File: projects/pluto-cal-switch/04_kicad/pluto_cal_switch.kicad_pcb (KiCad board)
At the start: 4 copper layers, 112 x 60 mm, 77 parts, among them Y1 C20625731

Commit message: the 50 ohm width was one method run twice, and the term that decides it is the solder mask nobody counted
RE-DERIVED INDEPENDENTLY BEFORE AUTHORING, because both existing
derivations were Hammerstad-Jensen closed form — one method twice, which
is the shared-method trap canon M1 names, not two agreeing sources.

METHOD: 2D finite-difference electrostatic field solve on the actual
cross-section. Box-integration discretisation of div(eps grad V)=0 on a
graded half-domain with a Neumann symmetry plane; charge by DISCRETE
GAUSS (Q = -eps0 * (A@V) over the conductor nodes), cross-checked against
the field-energy integral (agree to 1e-3). VALIDATED at t=0 against
Hammerstad-Jensen — where the closed form is uncontroversial — to
-0.29..-0.56 % over w/h 0.5..4.0. Outer box swept 40h->320h: 0.02 ohm, so
the residual is mesh, not truncation, and it CANCELS in a ratio.

THREE SOLVES OF w FOR 50.00 OHM AT Dk 4.4, h 0.2104, t 0.035:
  0.3610 mm  Hammerstad closed form, bare trace   (the two prior ones)
  0.3736 mm  THIS field solve,       bare trace   (mesh bias cancelled)
  0.3590 mm  THIS field solve,       AS FABBED
The first two are the SAME cross-section computed two ways and disagree
by 3.4 % — a wider spread than the correction being made. So "0.35 is not
50 ohm, therefore 0.361" does not follow: 0.361 is one method's answer to
a question the methods do not agree on.

WHAT BROKE THE TIE. Neither closed form carries the solder mask, and at
w 0.35 the mask is worth -1.55 ohm against a trapezoidal-etch term of
+0.46. A 1.55 ohm term omitted from a 0.8 ohm argument is the argument.
This board does not open mask over its RF runs, so as-fabbed is what the
copper will be.

0.36 mm AUTHORED because the two surviving models BRACKET it — 0.3590
(field solve, as fabbed) and 0.3610 (closed form, bare) differ by 2 um.
That is convergence once the geometry is complete, not averaging.

NOT INFLATED. Old width worst case RL 35.0 dB (best 43.4); new 39.8/62.5.
ADR-0010's own corrected figu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
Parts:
- R_HDR_G: value 3.3kΩ -> 2.2kΩ
- R_HDR_S: value 2.2kΩ -> 3.3kΩ
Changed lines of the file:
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@@
 			)
 		)
-		(property "Value" "2.2kΩ"
+		(property "Value" "3.3kΩ"
 			(at 0 1.17 0)
 			(layer "F.Fab")
@@
 			)
 		)
-		(property "Value" "3.3kΩ"
+		(property "Value" "2.2kΩ"
 			(at 0 1.17 0)
 			(layer "F.Fab")

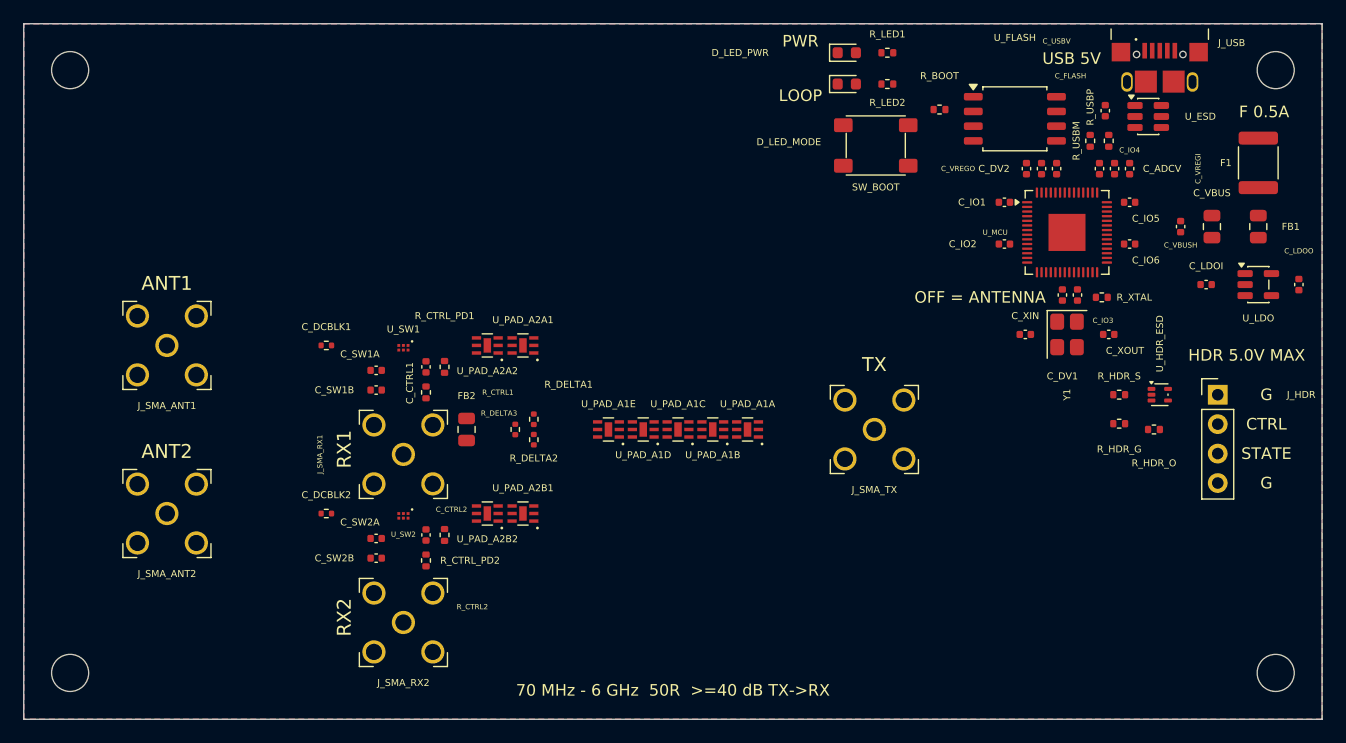
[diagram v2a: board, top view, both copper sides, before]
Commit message: seed_stubs finally runs through the pipeline, and the 67 mask findings were ONE aperture the datasheet requires
THE BLOCKER IS CONFIRMED GONE FROM THIS BOARD'S SIDE. prep -> route
(--race 4) -> import -> taps -> stitch now runs to EXIT 0 with
`seed_stubs: 21 pin(s) served, 32 segments placed, 0 refused` and NO hand
unfill anywhere; import logs "--no-fill" for itself. That is what makes
the recipe expressible in route.yaml, which is the whole reason the chain
was refused promotion yesterday (canon M3).

THE CHAIN IS STILL NOT PROMOTED AND route.final: IS STILL COMMENTED OUT.
The gate is 16 violations / 8 unconnected / 0 parity. Promoting a dirty
chain seals it. Same refusal as the predecessor, different epistemic
status: the residue is now CLASSIFIED, not inherited.

83 -> 16 VIOLATIONS, AND THE 67 THAT WENT WERE ONE DEFECT.
Every solder_mask_bridge finding (12 distinct pairs) was inside U_SW1 /
U_SW2 and was the SAME single mask aperture. That aperture is DELIBERATE
and the footprint's own descr already said so: BGS12WN6 Rev 2.9 Figure 5
gives six lands on a 0.40 mm grid with a 0.15 mm land-to-land gap, which
is below JLCPCB's 0.2 mm mask-dam minimum, so per-pad openings are
UNMANUFACTURABLE. Declared as `allow_soldermask_bridges` in the footprint
that OWNS the fact rather than waived in a downstream gate, because a
waiver needs evidence and an inherited waiver is an inherited defect.
Counting these 67 as findings would have been counting one datasheet
constraint sixty-seven times.

hole_to_hole 0.5 -> 0.25, AND IT IS ARITHMETIC, NOT A DENSITY TRADE.
Five escape vias walled in at 0.5 (measured gaps 0.282 / 0.350 / 0.373 /
0.404 / 0.450 mm) and the stitch gate refused the board on all five. All
five are LEGAL at the declared tier's published 0.25. Two adjacent escape
vias on the RP2040's 0.400 mm pitch at the tier's own 0.15 mm drill are
    pitch - drill = 0.400 - 0.150 = 0.250 mm apart, EXACTLY
so at a 0.5 floor EVERY adjacent-pin escape via on a QFN-56 was a
viola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
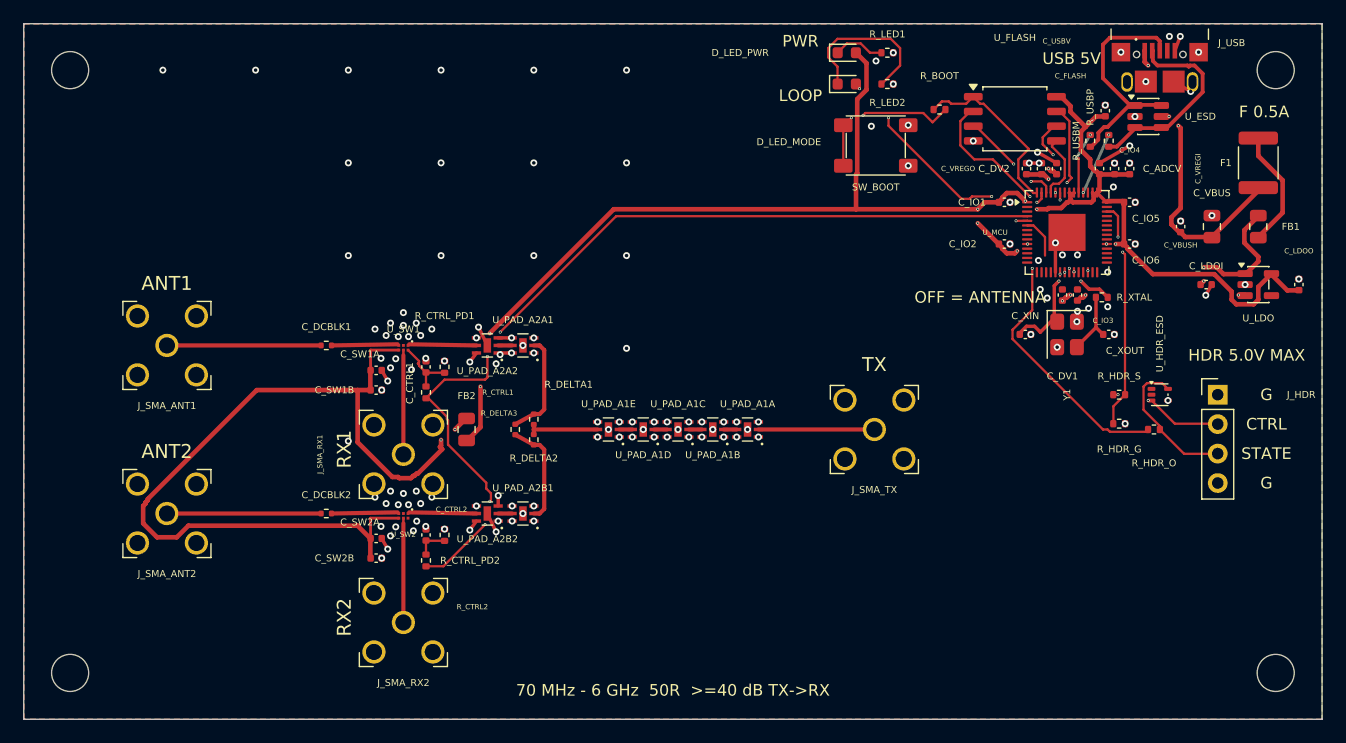
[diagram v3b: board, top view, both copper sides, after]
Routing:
- net 3V3: track 0.00 -> 149.1 mm, vias 0 -> 14
- net RF_CTRL: track 0.00 -> 80.2 mm, vias 0 -> 4
- net 3V3_SW: track 0.00 -> 76.3 mm, vias 0 -> 2
- net VBUS: track 0.00 -> 27.4 mm, vias 0 -> 3
- net HDR_STATE_GPIO: track 0.00 -> 25.5 mm, vias 0 -> 1
- net GND: track 0.00 -> 23.3 mm, vias 0 -> 144
- net LED_MODE: track 0.00 -> 20.4 mm, vias 0 -> 4
- net USB_DP: track 0.00 -> 20.3 mm
- net HDR_CTRL_ADC: track 0.00 -> 19.8 mm, vias 0 -> 2
- net VREG_VOUT: track 0.00 -> 17.9 mm, vias 0 -> 4
- net USB_DM: track 0.00 -> 17.6 mm
- net VBUS_F: track 0.00 -> 16.2 mm, vias 0 -> 3
- net QSPI_CSN: track 0.00 -> 15.7 mm
- net LED_MODE_K: track 0.00 -> 14.1 mm
- net USB_BOOT: track 0.00 -> 13.5 mm, vias 0 -> 2
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
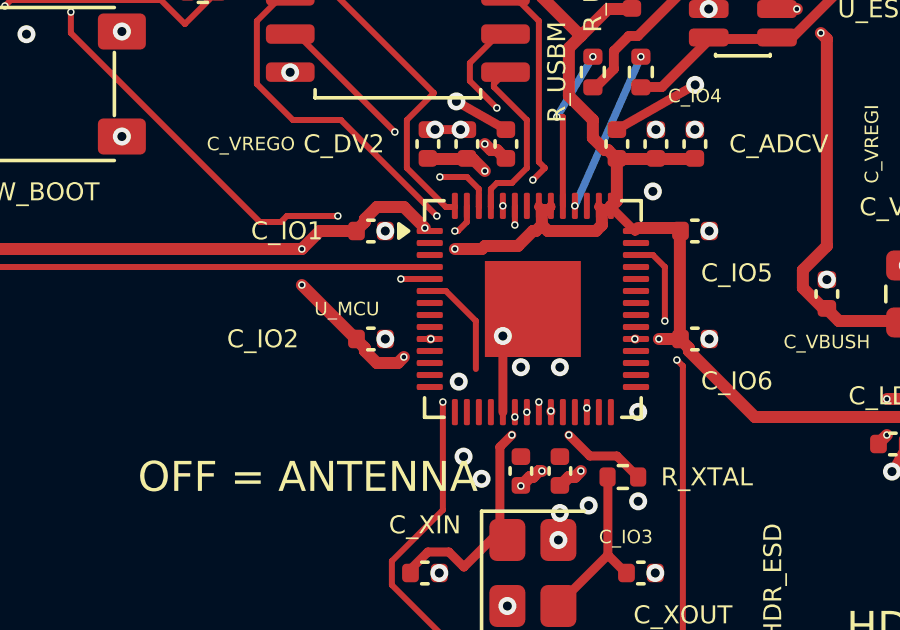
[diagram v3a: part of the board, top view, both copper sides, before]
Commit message: the eight track_width findings were eight DECLARED tap widths that nothing ever told DRC about
16 -> 8 violations. Every track_width finding is gone, and none of them
was a routing defect: all eight were widths `route.yaml taps:` DECLARES
explicitly, graded against netclass TRUNK floors they were never meant to
meet. A tap width is authored in route.yaml and a DRC floor is authored
in nets.yaml, and nothing joined the two — so the board was failing
itself for doing exactly what its own config said to do.

THREE RULE AREAS, ONE PER MEASURED CLASS, EACH THE BOUNDING BOX OF THE
COPPER IT LICENSES. Deliberately NOT a widening of the existing areas:
enlarging taper_u_sw1 would have relaxed RX_PLUTOn's impedance width, and
enlarging taper_u_mcu would have relaxed the whole 3V3 net across the
flash field. Scope is the evidence.

  tap_3v3_sw1 / tap_3v3_sw2 (4 findings) — U_SWn.4 -> C_SWnA.1, measured
  at (52.350,48.150)->(49.920,48.150)->(49.920,49.900) and its +14.5 mm
  twin. 0.25 mm against PWR's 0.400. BGS12WN6 pin 4 draws 125 uA MAXIMUM
  (Table 2), four orders under anything ampacity could ask, and PWR's 0.4
  is an IR-drop choice against a 0.10 A trunk this branch is not on.

  tap_usb_die (3 findings) — and it could not be folded into taper_u_mcu
  for TWO independent measured reasons, which is why it is its own area:
  the hop leaves F.Cu entirely (B.Cu runs (110.800,31.600)->(112.000,
  29.590) and (111.400,34.562)->(113.600,29.590)) while taper_u_mcu is
  F.Cu/In2.Cu, AND it reaches y 29.59, north of that area's y0 = 33.00.

  Its floor is 0.20, not 0.25, and the 0.05 is MEASURED not chosen: the
  tap is declared at 0.25 and two F.Cu segments come out at 0.200 because
  U_MCU.47 is itself a 0.200 mm land and the threader leaves a pad at the
  pad's width. Extending stitch.width_floor's region to lift them was
  REJECTED — it would also widen every 3V3 and VREG_VOUT track in the
  flash/decoupling field into the most congested area on the board to
  satisfy a co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
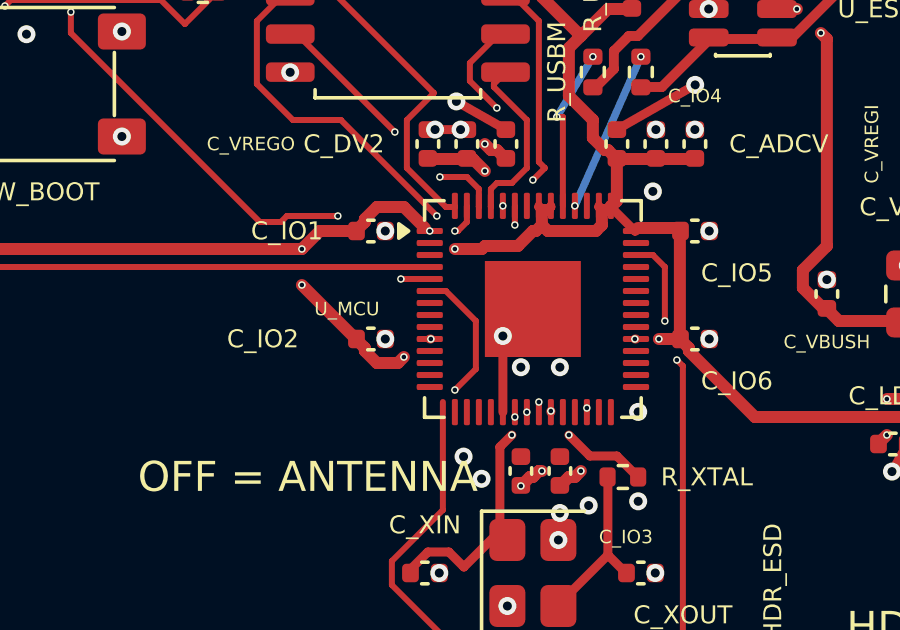
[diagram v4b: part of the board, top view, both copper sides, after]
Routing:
- net HDR_STATE_GPIO: track 25.5 -> 26.4 mm
- net GND: vias 144 -> 143
